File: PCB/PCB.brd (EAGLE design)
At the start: 428.5 x 124 mm, 216 parts, among them J3 Boot, Q1 FS8205A, U1 ESP32-S3HOLE

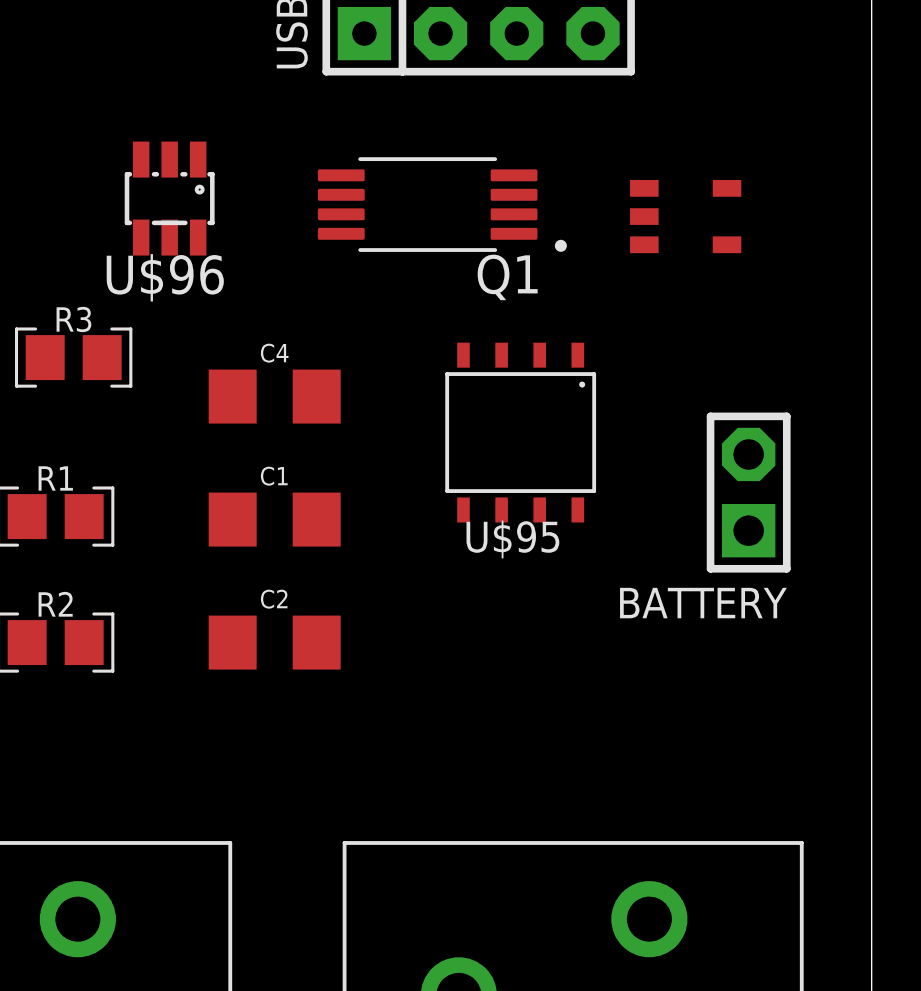
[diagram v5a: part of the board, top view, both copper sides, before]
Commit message: Finished the power circuit for the keyboard
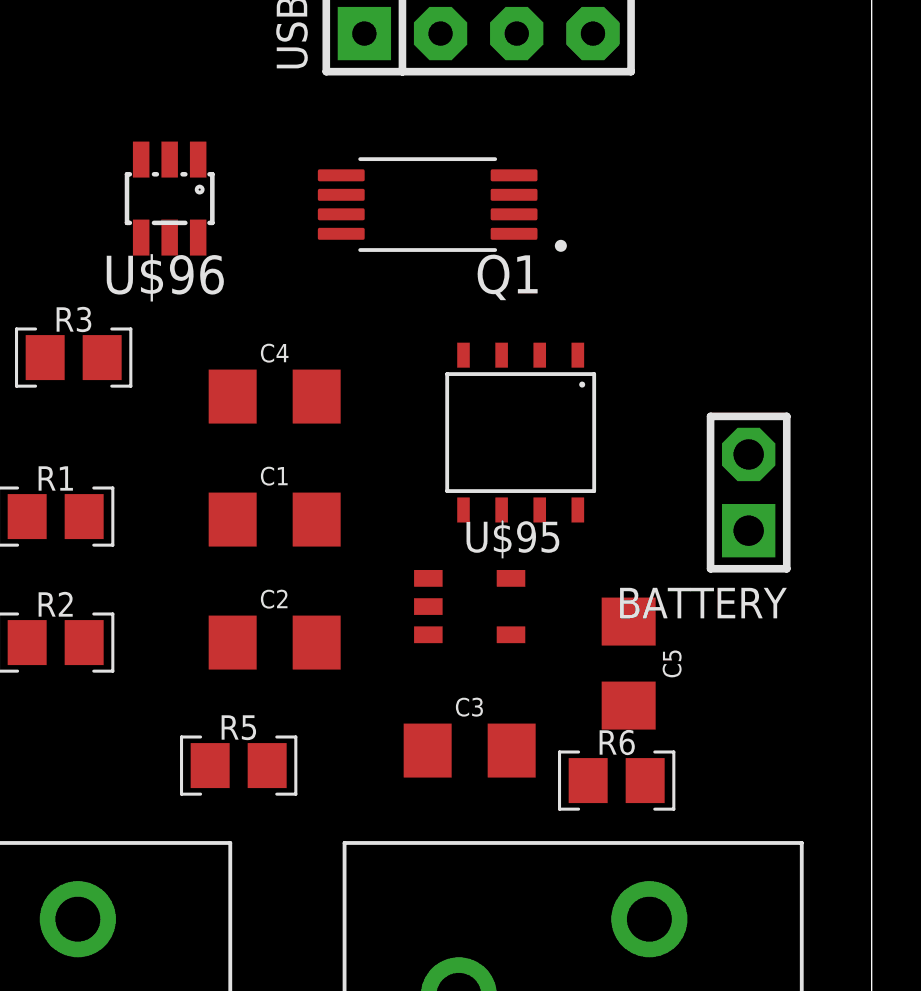
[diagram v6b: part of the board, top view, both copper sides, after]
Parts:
- removed REGULATOR: RT9080-33GJ5, RT9080:TSOT-23-5_RIT
- added C3, C5: 1.0uF, SparkFun-Capacitors:1206
- added R5: 1M, resistors:R-0805
- added R6: 8200000, resistors:R-0805
- added U2: ME6211C33M5G, ME6211:ME6211C33M5G
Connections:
- removed net VIN: REGULATOR.1
- new net B+: BATTERY.2, C1.1, C3.1, R2.2, R5.1, U$95.5, U2.1, U2.3
- new net N$35: R5.2, R6.1
- net GND: now also C3.2, C5.2, R6.2, U2.2
- net VCC: now also C5.1, U2.5; no longer BATTERY.2, C1.1, R2.2, U$95.5
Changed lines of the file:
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@@
 <attribute name="NAME" x="372.93" y="119.895" size="1.016" layer="25" ratio="18"/>
-</element>
-<element name="REGULATOR" library="RT9080" package="TSOT-23-5_RIT" value="RT9080-33GJ5" x="424.8" y="117" smashed="yes">
-<attribute name="COPYRIGHT" value="Copyright (C) 2023 Ultra Librarian. All rights reserved." x="424.8" y="117" size="1.778" layer="27" display="off"/>
-<attribute name="MANUFACTURER_PART_NUMBER" value="RT9080-33GJ5" x="424.8" y="117" size="1.778" layer="27" display="off"/>
-<attribute name="MFR_NAME" value="Richtek Technology" x="424.8" y="117" size="1.778" layer="27" display="off"/>
-<attribute name="NAME" x="423.1634" y="118.905" size="0.762" layer="27" ratio="6" rot="SR0"/>
-<attribute name="VALUE" x="423.1428" y="114.395" size="0.762" layer="27" ratio="6" rot="SR0"/>
 </element>
 <element name="R2" library="resistors" package="R-0805" value="1K" x="403.8" y="102.8" smashed="yes">
@@
 <attribute name="VALUE" x="411.1" y="101.657" size="0.6096" layer="27" font="vector" ratio="20" align="top-center"/>
 </element>
+<element name="R5" library="resistors" package="R-0805" value="1M" x="409.9" y="98.7" smashed="yes">
+<attribute name="MOUSER" value="660-RK73H2ATTD1001F" x="410.3" y="98.7" size="1.778" layer="27" display="off"/>
+<attribute name="NAME" x="409.9" y="99.97" size="0.8128" layer="25" ratio="15" rot="R180" align="center"/>
+</element>
+<element name="R6" library="resistors" package="R-0805" value="8200000" x="422.5" y="98.2" smashed="yes">
+<attribute name="MOUSER" value="660-RK73H2ATTD1001F" x="422.9" y="98.2" size="1.778" layer="27" display="off"/>
+<attribute name="NAME" x="422.5" y="99.47" size="0.8128" layer="25" ratio="15" rot="R180" align="center"/>
+</element>
+<element name="U2" library="ME6211" package="ME6211C33M5G" value="ME6211C33M5G" x="417.6" y="104" smashed="yes">
+<attribute name="COPYRIGHT" value="Copyright (C) 2023 Ultra Librarian. All rights reserved." x="417.6" y="104" size="1.778" layer="27" display="off"/>
+<attribute name="MANUFACTURER_PART_NUMBER" value="RT9080-33GJ5" x="417.6" y="104" size="1.778" layer="27" display="off"/>
+<attribute name="MFR_NAME" value="Richtek Technology" x="417.6" y="104" size="1.778" layer="27" display="off"/>
+<attribute name="NAME" x="415.9634" y="105.905" size="0.762" layer="27" ratio="6" rot="SR0"/>
+<attribute name="VALUE" x="415.9428" y="101.395" size="0.762" layer="27" ratio="6" rot="SR0"/>
+</element>
+<element name="C3" library="SparkFun-Capacitors" package="1206" value="1.0uF" x="417.6" y="99.2" smashed="yes">
+<attribute name="NAME" x="417.6" y="100.343" size="0.6096" layer="25" font="vector" ratio="20" align="bottom-center"/>
+<attribute name="PROD_ID" value="CAP-09822" x="417.6" y="99.2" size="1.778" layer="27" display="off"/>
+<attribute name="VALUE" x="417.6" y="98.057" size="0.6096" layer="27" font="vector" ratio="20" align="top-center"/>
+</element>
+<element name="C5" library="SparkFun-Capacitors" package="1206" value="1.0uF" x="422.9" y="102.1" smashed="yes" rot="R270">
+<attribute name="NAME" x="424.043" y="102.1" size="0.6096" layer="25" font="vector" ratio="20" rot="R270" align="bottom-center"/>
+<attribute name="PROD_ID" value="CAP-09822" x="422.9" y="102.1" size="1.778" layer="27" rot="R270" display="off"/>
+<attribute name="VALUE" x="421.757" y="102.1" size="0.6096" layer="27" font="vector" ratio="20" rot="R270" align="top-center"/>
+</element>
 </elements>
 <signals>
@@
 <contactref element="U1" pad="40"/>
 <contactref element="U1" pad="1"/>
+<contactref element="R6" pad="2"/>
+<contactref element="C5" pad="2"/>
+<contactref element="C3" pad="2"/>
+<contactref element="U2" pad="2"/>
 <wire x1="357.05" y1="122.9" x2="374.11" y2="122.5" width="0" layer="19" extent="1-1"/>
 <wire x1="338.5809" y1="119.2537" x2="357.05" y2="122.9" width="0" layer="19" extent="1-1"/>
@@
 <wire x1="421.205" y1="112.38" x2="418.665" y2="112.38" width="0" layer="19" extent="1-1"/>
 <wire x1="224.84" y1="15.04" x2="302.045" y2="105.115" width="0" layer="19" extent="1-1"/>
+<wire x1="423.45" y1="98.2" x2="224.84" y2="15.04" width="0" layer="19" extent="1-1"/>
+<wire x1="419" y1="99.2" x2="423.45" y2="98.2" width="0" layer="19" extent="1-1"/>
+<wire x1="422.9" y1="100.7" x2="419" y2="99.2" width="0" layer="19" extent="1-1"/>
+<wire x1="416.22205" y1="104" x2="419" y2="99.2" width="0" layer="19" extent="1-1"/>
 </signal>
 <signal name="SCK">
@@
 <contactref element="J3" pad="2"/>
 <contactref element="U$94" pad="24"/>
-<contactref element="U$95" pad="5"/>
-<contactref element="BATTERY" pad="2"/>
-<contactref element="R2" pad="2"/>
 <contactref element="R4" pad="1"/>
-<contactref element="C1" pad="1"/>
 <contactref element="SCREEN" pad="2"/>
 <contactref element="U1" pad="2"/>
-<wire x1="409.7" y1="106.9" x2="404.75" y2="102.8" width="0" layer="19" extent="1-1"/>
-<wire x1="417.395" y1="107.22" x2="409.7" y2="106.9" width="0" layer="19" extent="1-1"/>
-<wire x1="426.9" y1="109.07" x2="417.395" y2="107.22" width="0" layer="19" extent="1-1"/>
-<wire x1="376.65" y1="122.5" x2="404.75" y2="102.8" width="0" layer="19" extent="1-1"/>
+<contactref element="U2" pad="5"/>
+<contactref element="C5" pad="1"/>
 <wire x1="354.51" y1="122.9" x2="376.65" y2="122.5" width="0" layer="19" extent="1-1"/>
 <wire x1="355.05" y1="113.1" x2="354.51" y2="122.9" width="0" layer="19" extent="1-1"/>
 <wire x1="321.4191" y1="117.9837" x2="354.51" y2="122.9" width="0" layer="19" extent="1-1"/>
 <wire x1="311.355" y1="119.085" x2="321.4191" y2="117.9837" width="0" layer="19" extent="1-1"/>
+<wire x1="418.97795" y1="104.9398" x2="311.355" y2="119.085" width="0" layer="19" extent="1-1"/>
+<wire x1="422.9" y1="103.5" x2="418.97795" y2="104.9398" width="0" layer="19" extent="1-1"/>
 </signal>
 <signal name="RX">
@@
 <wire x1="409.7" y1="102.8" x2="402.85" y2="102.8" width="0" layer="19" extent="1-1"/>
 </signal>
-<signal name="VIN">
-<contactref element="REGULATOR" pad="1"/>
-</signal>
 <signal name="SCL">
 <contactref element="SCREEN" pad="3"/>
@@
 <contactref element="U1" pad="27"/>
 </signal>
+<signal name="B+">
+<contactref element="U$95" pad="5"/>
+<contactref element="R2" pad="2"/>
+<contactref element="C1" pad="1"/>
+<contactref element="BATTERY" pad="2"/>
+<contactref element="C3" pad="1"/>
+<contactref element="U2" pad="1"/>
+<contactref element="R5" pad="1"/>
+<contactref element="U2" pad="3"/>
+<wire x1="409.7" y1="106.9" x2="404.75" y2="102.8" width="0" layer="19" extent="1-1"/>
+<wire x1="417.395" y1="107.22" x2="409.7" y2="106.9" width="0" layer="19" extent="1-1"/>
+<wire x1="426.9" y1="109.07" x2="417.395" y2="107.22" width="0" layer="19" extent="1-1"/>
+<wire x1="408.95" y1="98.7" x2="404.75" y2="102.8" width="0" layer="19" extent="1-1"/>
+<wire x1="416.22205" y1="104.9398" x2="408.95" y2="98.7" width="0" layer="19" extent="1-1"/>
+<wire x1="416.22205" y1="103.0602" x2="416.22205" y2="104.9398" width="0" layer="19" extent="1-1"/>
+<wire x1="416.2" y1="99.2" x2="416.22205" y2="103.0602" width="0" layer="19" extent="1-1"/>
+</signal>
+<signal name="N$35">
+<contactref element="R6" pad="1"/>
+<contactref element="R5" pad="2"/>
+<wire x1="410.85" y1="98.7" x2="421.55" y2="98.2" width="0" layer="19" extent="1-1"/>
+</signal>
 </signals>

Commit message: Finished .sch
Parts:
- removed J3: Boot, con-headers-jp:SIP-100-06-32
- removed RXTX: F-1X02-SIP-100-40, con-headers-jp:SIP-100-02-40
- added BOOT: BOOT, con-headers-jp:SIP-100-04-32
- added BUTTON1: 1, switch-omron:B3F-10XX
- added R7: 1K, resistors:R-0805
- added U$67: WS2812B5050, Led-WS2812B:WS2812B5050
- BUTTON: value (none) -> 1
- moved R4 5.85 mm to (357.7, 118.7), turned to 180 degrees
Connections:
- removed net MISO: J3.5
- removed net MOSI: J3.4
- removed net RESET: BUTTON.4, J3.3, R4.2
- removed net SCK: J3.6
- new net N$79: U$67.LED_VDD
- net BATLEVEL: now also R5.2, R6.1
- net D+: now also U1.14
- net D-: now also U1.13
- net EN: now also BUTTON1.4, R7.2
- net GND: now also BOOT.1, BUTTON1.1; no longer J3.1
- net LEDS: now also U$67.LED_DI
- net N$35: now also U$67.LED_GND; no longer R5.2, R6.1
- net PROG: now also BUTTON.4, R4.2
- net RX: now also BOOT.4; no longer RXTX.1
- net STDBY: now also U1.23
- net TX: now also BOOT.3; no longer RXTX.2
- net VCC: now also BOOT.2, R7.1; no longer J3.2
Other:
- board text removed: "GND"
- board text removed: "MISO"
- board text removed: "MOSI"
- board text removed: "RESET"
- board text removed: "SCK"
- board text removed: "VCC"

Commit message: Added new holes and changed the pcb layaout to fit the usb connector
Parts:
- moved USB 68.4 mm to (349.6, 119.7)
- moved BOOT 43.5 mm to (306.8, 123.7)
- moved R4 3.94 mm to (361.2, 116.9)
- moved U$95 0.30 mm to (419.3, 110.1)
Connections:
- removed net N$35: U$67.LED_GND
- removed net N$79: U$67.LED_VDD
- net GND: now also U$67.LED_GND
- net VCC: now also U$67.LED_VDD
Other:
- outline, holes or cut-outs redrawn
